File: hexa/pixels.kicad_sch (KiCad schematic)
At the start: 291 parts

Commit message: add pads for new hexa controller and add to hexa with fresh layout; todo proper routing around the new controller footprint
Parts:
- renumbered D1 to D124, D2 to D125, D3 to D126, D4 to D127, D5 to D128, D6 to D129, D7 to D130, D8 to D131, D9 to D132, D10 to D133, D11 to D134, D12 to D135, D13 to D136, D14 to D137, D15 to D138, D16 to D139, D17 to D140, D18 to D141, D19 to D142, D20 to D143, D21 to D144, D22 to D145, D23 to D146, D24 to D147, D25 to D148, D26 to D149, D27 to D150, D28 to D151, D29 to D152, D30 to D153, D31 to D154, D32 to D155, D33 to D156, D34 to D157, D35 to D158, D36 to D159, D37 to D160, D38 to D161, D39 to D162, D40 to D163, D41 to D164, D42 to D165, D43 to D166, D44 to D167, D45 to D168, D46 to D169, D47 to D170, D48 to D171, D49 to D172, D50 to D173, D51 to D174, D52 to D175, D53 to D176, D54 to D177, D55 to D178, D56 to D179, D57 to D180, D58 to D181, D59 to D182, D60 to D183, D61 to D184, D62 to D185, D63 to D186, D64 to D187, D65 to D188, D66 to D189, D67 to D190, D68 to D191, D69 to D192, D70 to D193, D71 to D194, D72 to D195, D73 to D196, D74 to D197, D75 to D198, D76 to D199, D77 to D200, D78 to D201, D79 to D202, D80 to D203, D81 to D204, D82 to D205, D83 to D206, D84 to D207, D85 to D208, D86 to D209, D87 to D210, D88 to D211, D89 to D212, D90 to D213

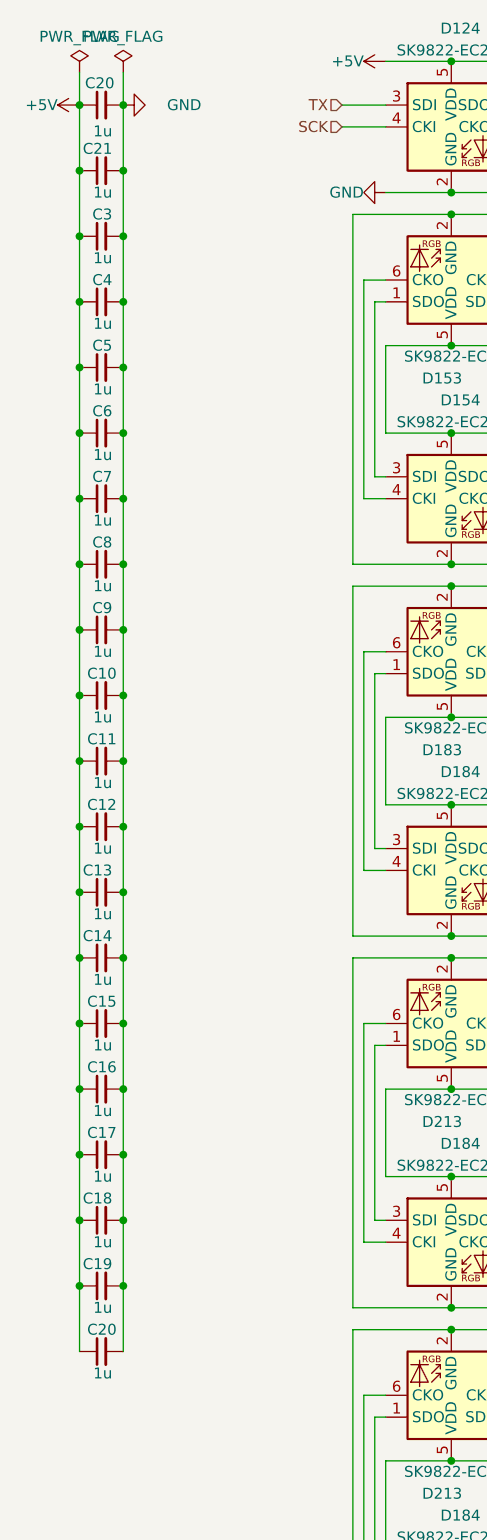
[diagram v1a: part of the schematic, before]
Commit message: make hexa capacitors 10u instead of 1u. I would have sworn this is how they were already, but nope. first run used 1u.
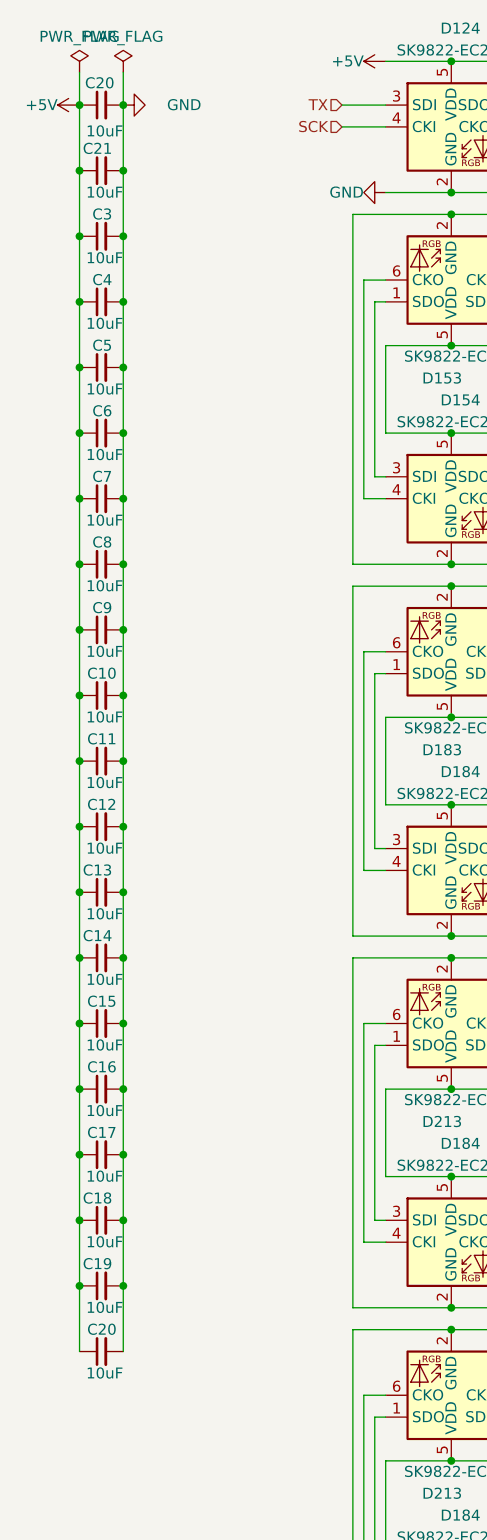
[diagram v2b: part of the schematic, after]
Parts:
- C10, C11, C12, C13, C14, C15, C16, C17, C18, C19, C20, C21, C3, C4, C5, C6, C7, C8, C9: value 1u -> 10uF
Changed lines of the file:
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@@
 			)
 		)
-		(property "Value" "1u"
-			(at -3.81 177.8 90)
+		(property "Value" "10uF"
+			(at -2.54 177.8 90)
 			(effects
 				(font
@@
 			)
 		)
-		(property "Value" "1u"
-			(at -3.81 63.5 90)
+		(property "Value" "10uF"
+			(at -2.54 63.5 90)
 			(effects
 				(font
@@
 			)
 		)
-		(property "Value" "1u"
-			(at -3.81 55.88 90)
+		(property "Value" "10uF"
+			(at -2.54 55.88 90)
 			(effects
 				(font
@@
 			)
 		)
-		(property "Value" "1u"
-			(at -3.81 78.74 90)
+		(property "Value" "10uF"
+			(at -2.54 78.74 90)
 			(effects
 				(font
@@
 			)
 		)
-		(property "Value" "1u"
-			(at -3.81 93.98 90)
+		(property "Value" "10uF"
+			(at -2.54 93.98 90)
 			(effects
 				(font
@@
 			)
 		)
-		(property "Value" "1u"
-			(at -3.81 147.32 90)
+		(property "Value" "10uF"
+			(at -2.54 147.32 90)
 			(effects
 				(font
@@
 			)
 		)
-		(property "Value" "1u"
-			(at -3.81 116.84 90)
+		(property "Value" "10uF"
+			(at -2.54 116.84 90)
 			(effects
 				(font
@@
 			)
 		)
-		(property "Value" "1u"
-			(at -3.81 154.94 90)
+		(property "Value" "10uF"
+			(at -2.54 154.94 90)
 			(effects
 				(font
@@
 			)
 		)
-		(property "Value" "1u"
-			(at -3.81 124.46 90)
+		(property "Value" "10uF"
+			(at -2.54 124.46 90)
 			(effects
 				(font
@@
 			)
 		)
-		(property "Value" "1u"
-			(at -3.81 71.12 90)
+		(property "Value" "10uF"
+			(at -2.54 71.12 90)
 			(effects
 				(font
@@
 			)
 		)
-		(property "Value" "1u"
-			(at -3.81 86.36 90)
+		(property "Value" "10uF"
+			(at -2.54 86.36 90)
 			(effects
 				(font
@@
 			)
 		)
-		(property "Value" "1u"
-			(at -3.81 162.56 90)
+		(property "Value" "10uF"
+			(at -2.54 162.56 90)
 			(effects
 				(font
@@
 			)
 		)
-		(property "Value" "1u"
-			(at -3.81 33.528 90)
+		(property "Value" "10uF"
+			(at -2.54 33.528 90)
 			(effects
 				(font
@@
 			)
 		)
-		(property "Value" "1u"
-			(at -3.81 40.64 90)
+		(property "Value" "10uF"
+			(at -2.54 40.64 90)
 			(effects
 				(font
@@
 			)
 		)
-		(property "Value" "1u"
-			(at -3.81 139.7 90)
+		(property "Value" "10uF"
+			(at -2.54 139.7 90)
 			(effects
 				(font
@@
 			)
 		)
-		(property "Value" "1u"
-			(at -3.81 48.26 90)
+		(property "Value" "10uF"
+			(at -2.54 48.26 90)
 			(effects
 				(font
@@
 			)
 		)
-		(property "Value" "1u"
-			(at -3.81 101.6 90)
+		(property "Value" "10uF"
+			(at -2.54 101.6 90)
 			(effects
 				(font
@@
 			)
 		)
-		(property "Value" "1u"
-			(at -3.81 109.22 90)
+		(property "Value" "10uF"
+			(at -2.54 109.22 90)
 			(effects
 				(font
@@
 			)
 		)
-		(property "Value" "1u"
-			(at -3.81 132.08 90)
+		(property "Value" "10uF"
+			(at -2.54 132.08 90)
 			(effects
 				(font
@@
 			)
 		)
-		(property "Value" "1u"
-			(at -3.81 170.18 90)
+		(property "Value" "10uF"
+			(at -2.54 170.18 90)
 			(effects
 				(font
